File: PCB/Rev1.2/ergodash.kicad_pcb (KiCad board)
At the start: 2 copper layers, 149.9 x 127.4 mm, 187 parts, among them J1 5PIN, J2 Conn_01x03, J3 Conn_01x03, J4 GS3, J5 GS3, M1 Speaker, Q1 IRLML6344TRPbF, SW1 SW_PUSH, SW10 SW_PUSH, SW11 SW_PUSH, SW12 SW_PUSH, SW13 SW_PUSH, SW14 SW_PUSH, SW15 SW_PUSH, SW16 SW_PUSH, SW17 SW_PUSH, SW18 SW_PUSH, SW19 SW_PUSH, SW2 SW_PUSH, SW20 SW_PUSH, SW21 SW_PUSH, SW22 SW_PUSH, SW23 SW_PUSH, SW24 SW_PUSH, SW25 SW_PUSH, SW26 SW_PUSH, SW27 SW_PUSH, SW28 SW_PUSH, SW29 SW_Push, SW3 SW_PUSH, SW30 SW_PUSH, SW31 SW_PUSH, SW32 SW_PUSH, SW33 SW_PUSH, SW34 SW_PUSH, SW35 SW_PUSH, SW36 SW_PUSH, SW37 SW_Push, SW38 SW_PUSH, SW39 SW_PUSH, SW4 SW_PUSH, SW40 SW_PUSH, SW41 SW_PUSH, SW5 SW_PUSH, SW6 SW_PUSH, SW7 SW_PUSH, SW8 SW_PUSH, SW9 SW_PUSH, U1 HOLE, U2 HOLE, U3 ProMicro, U4 HOLE, U5 HOLE, U6 ProMicro, U7 HOLE, U8 HOLE, U9 HOLE

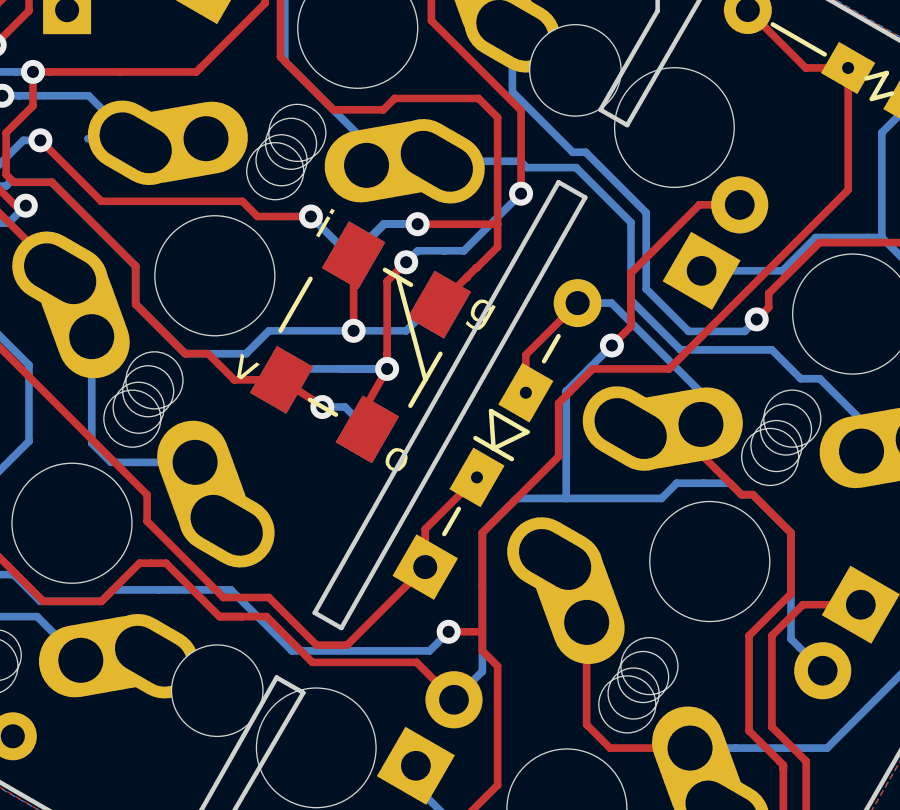
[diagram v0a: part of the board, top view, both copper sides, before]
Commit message: Increase thickness of connection to optional thumb pads and update EESchema symbols
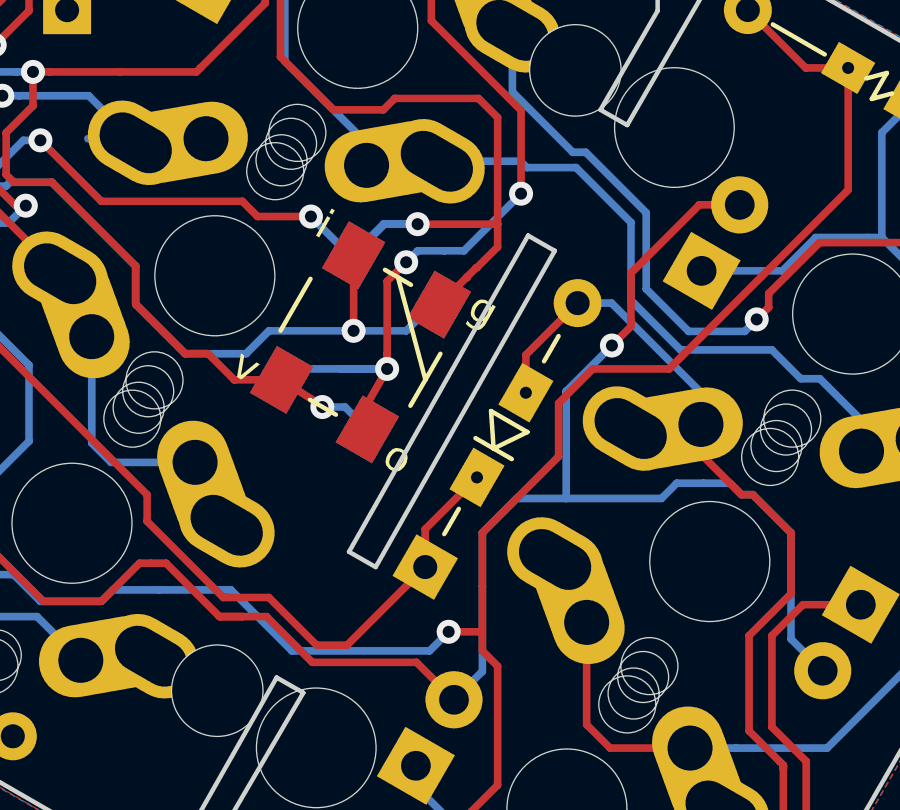
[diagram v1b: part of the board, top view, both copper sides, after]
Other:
- outline, holes or cut-outs redrawn

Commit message: Convert to Kicad 6
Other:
- net class Default removed
